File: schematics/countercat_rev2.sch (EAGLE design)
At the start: 67 parts, among them IC1 74LS595N, Q1 IRF520, Q2 2N3904, Q3 IRF520, Q4 IRF520, Q5 IRF520, U4 ATMEGA328P_PDIP, U6 RELAYPTH3, Y1 16MHz

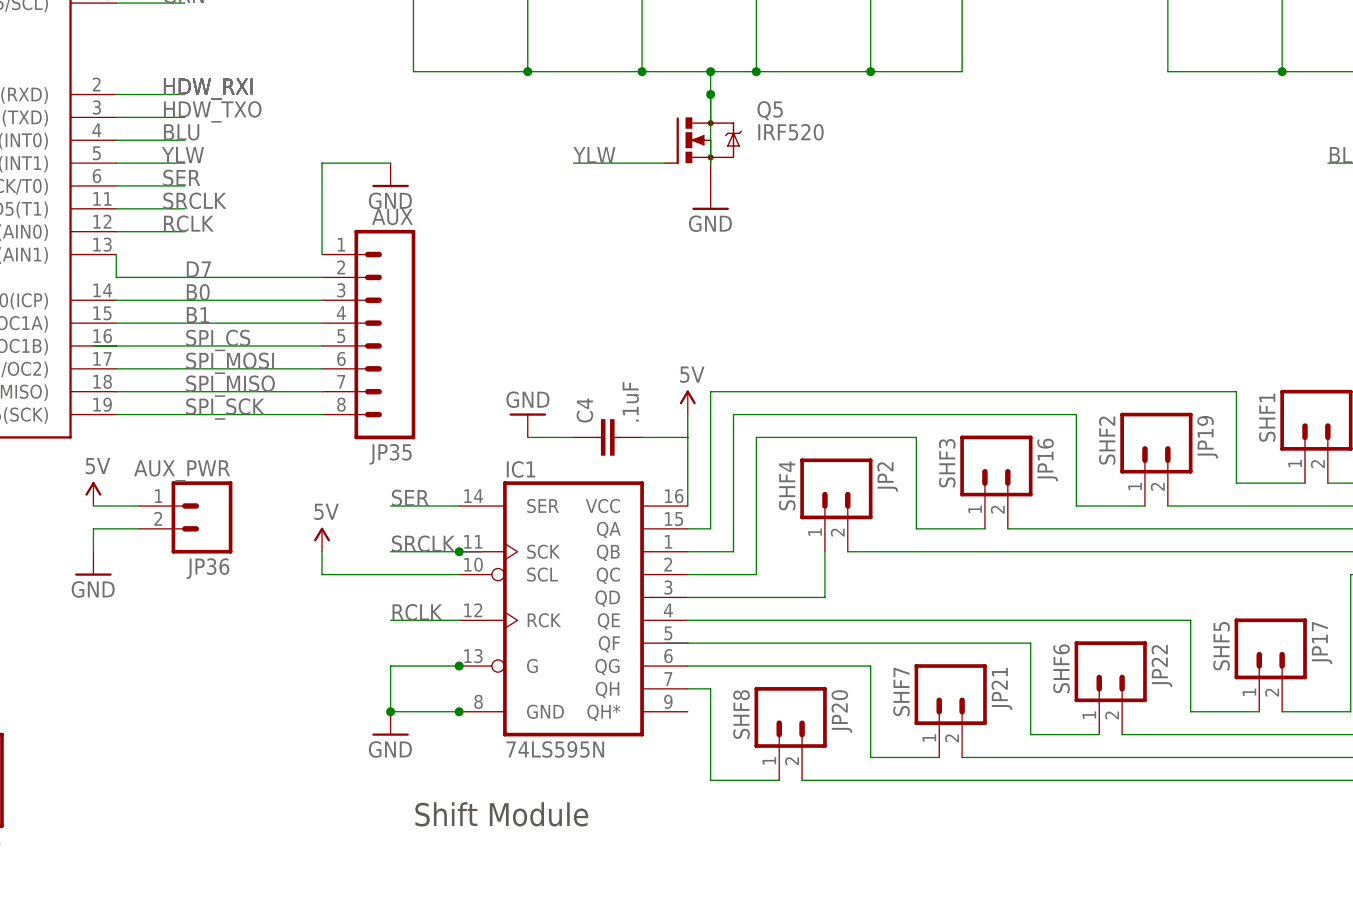
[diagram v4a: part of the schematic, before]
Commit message: Autorouted and DRC'd
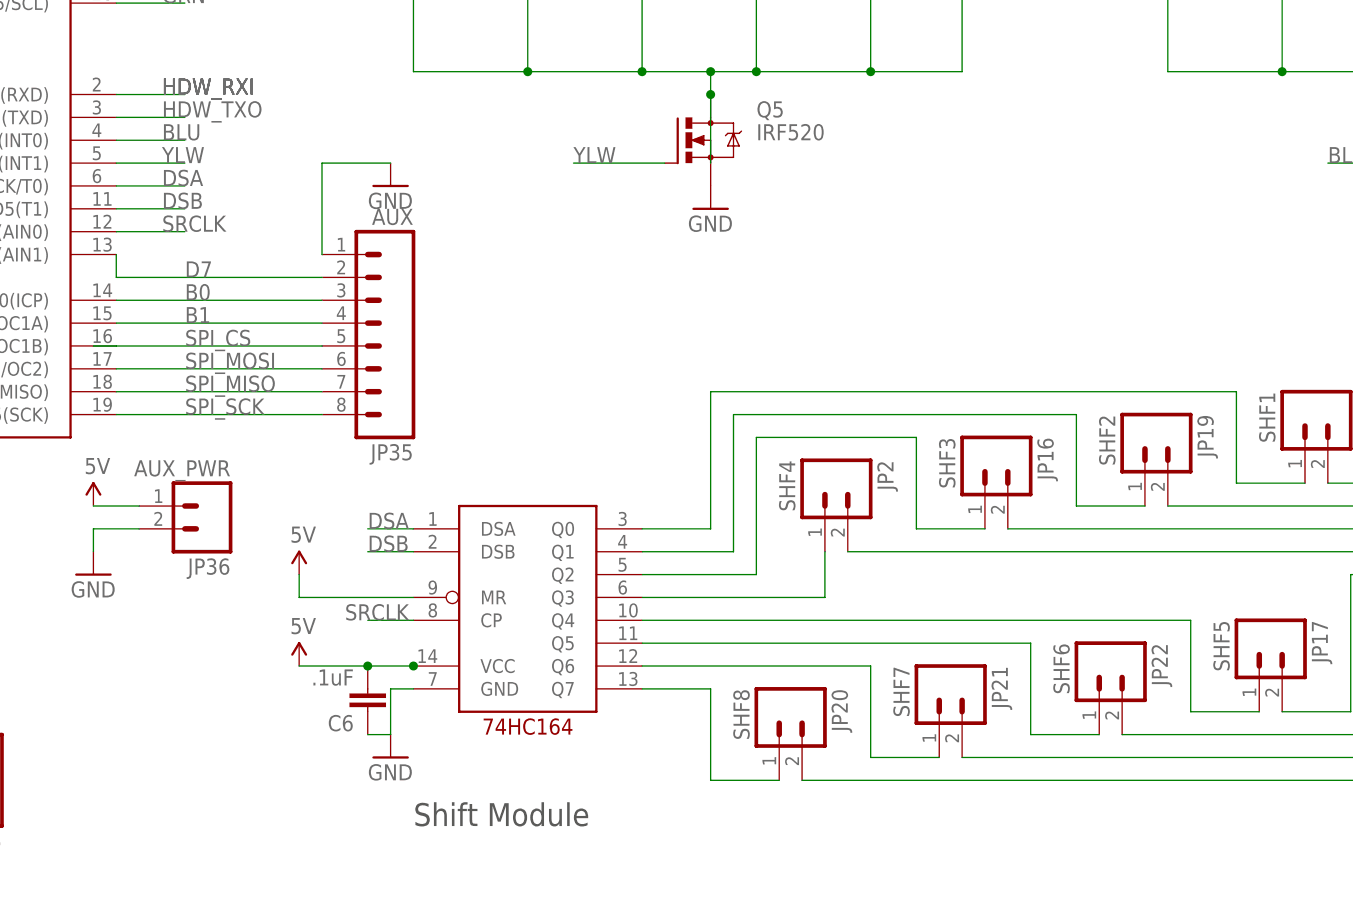
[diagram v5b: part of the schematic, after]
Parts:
- removed C4: .1uF, SparkFun-Capacitors:CAPPTH2
- removed IC1: 74LS595N, SparkFun-DigitalIC:74LS595N
- added C6: .1uF, SparkFun-Capacitors:CAPPTH2
- added U$15: 74XX164, andrews_eagle_lib:74XX164
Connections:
- removed net RCLK: IC1.RCK, U4.PD6(AIN0)
- removed net SER: IC1.SER, U4.PD4(XCK/T0)
- new net DSA: U$15.DSA, U4.PD4(XCK/T0)
- new net DSB: U$15.DSB, U4.PD5(T1)
- net 5V: now also C6.2, U$15.MR, U$15.VCC; no longer C4.2, IC1.SCL, IC1.VCC
- net GND: now also C6.1, U$15.GND; no longer C4.1, IC1.G, IC1.GND
- net N$1: now also U$15.Q4; no longer IC1.QE
- net N$26: now also U$15.Q0; no longer IC1.QA
- net N$27: now also U$15.Q1; no longer IC1.QB
- net N$28: now also U$15.Q2; no longer IC1.QC
- net N$29: now also U$15.Q3; no longer IC1.QD
- net N$30: now also U$15.Q6; no longer IC1.QG
- net N$31: now also U$15.Q5; no longer IC1.QF
- net N$32: now also U$15.Q7; no longer IC1.QH
- net SRCLK: now also U$15.CP, U4.PD6(AIN0); no longer IC1.SCK, U4.PD5(T1)

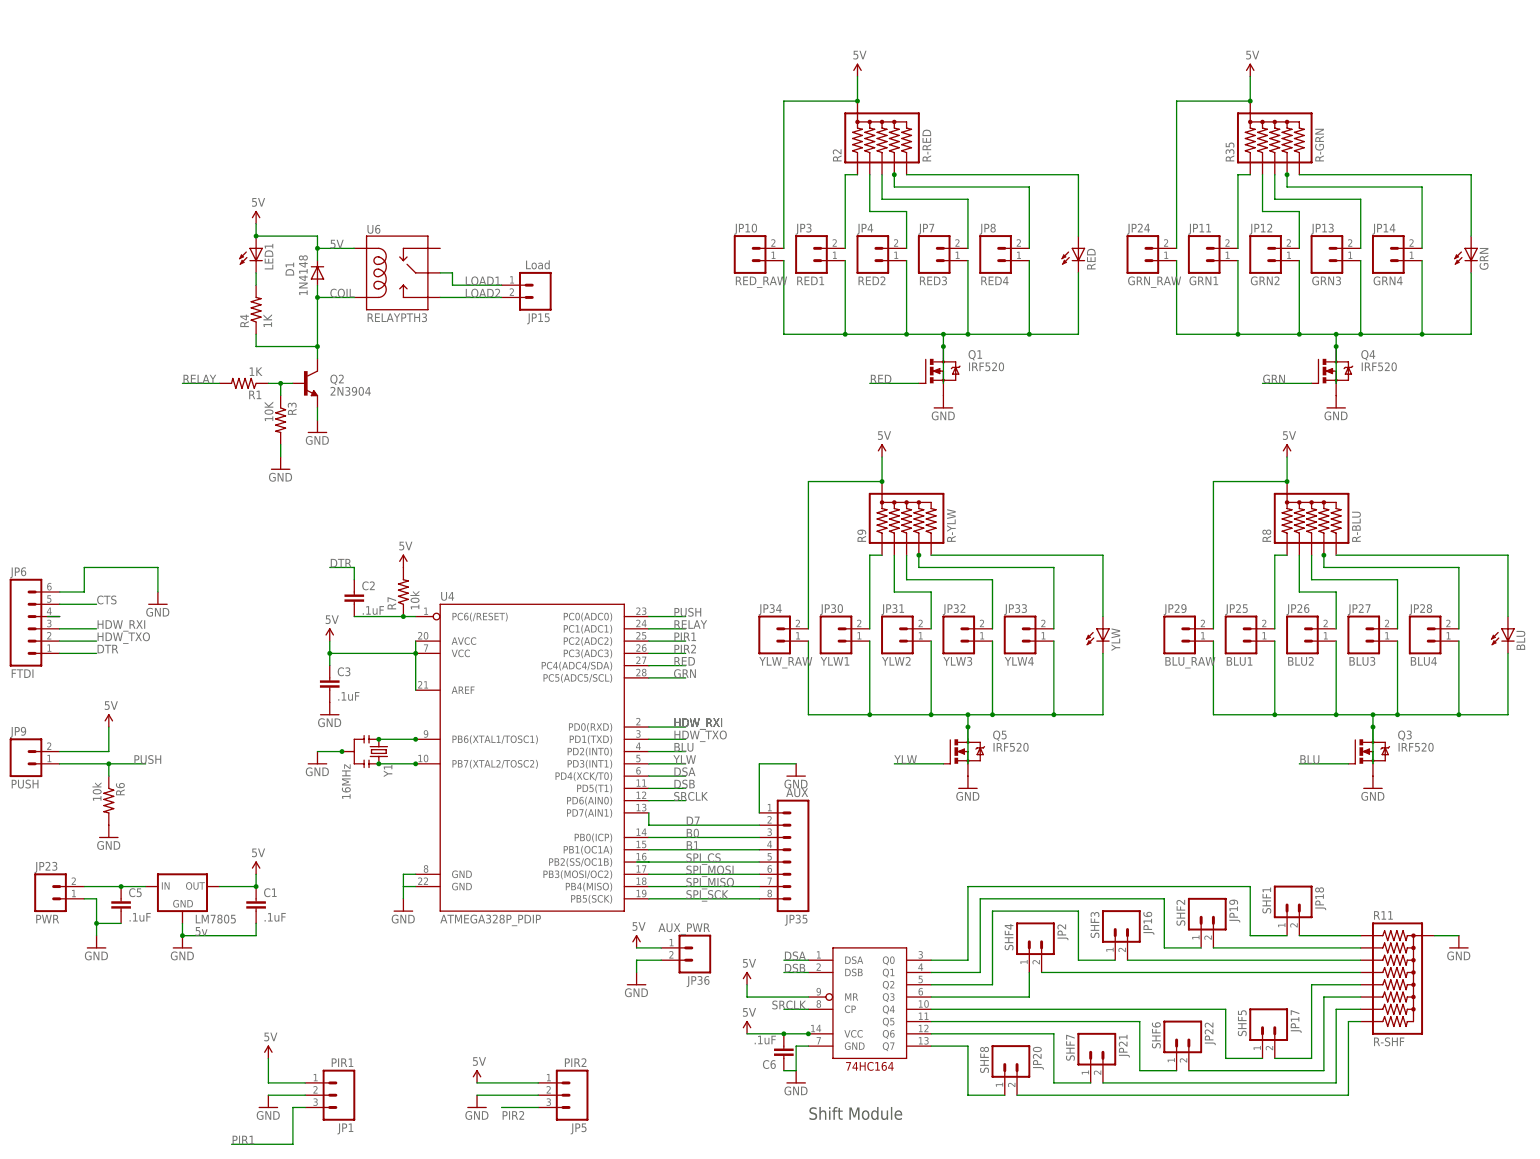
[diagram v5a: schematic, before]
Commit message: Got rid of relay on board. Made smaller, swapepd out shift reg. for decoder
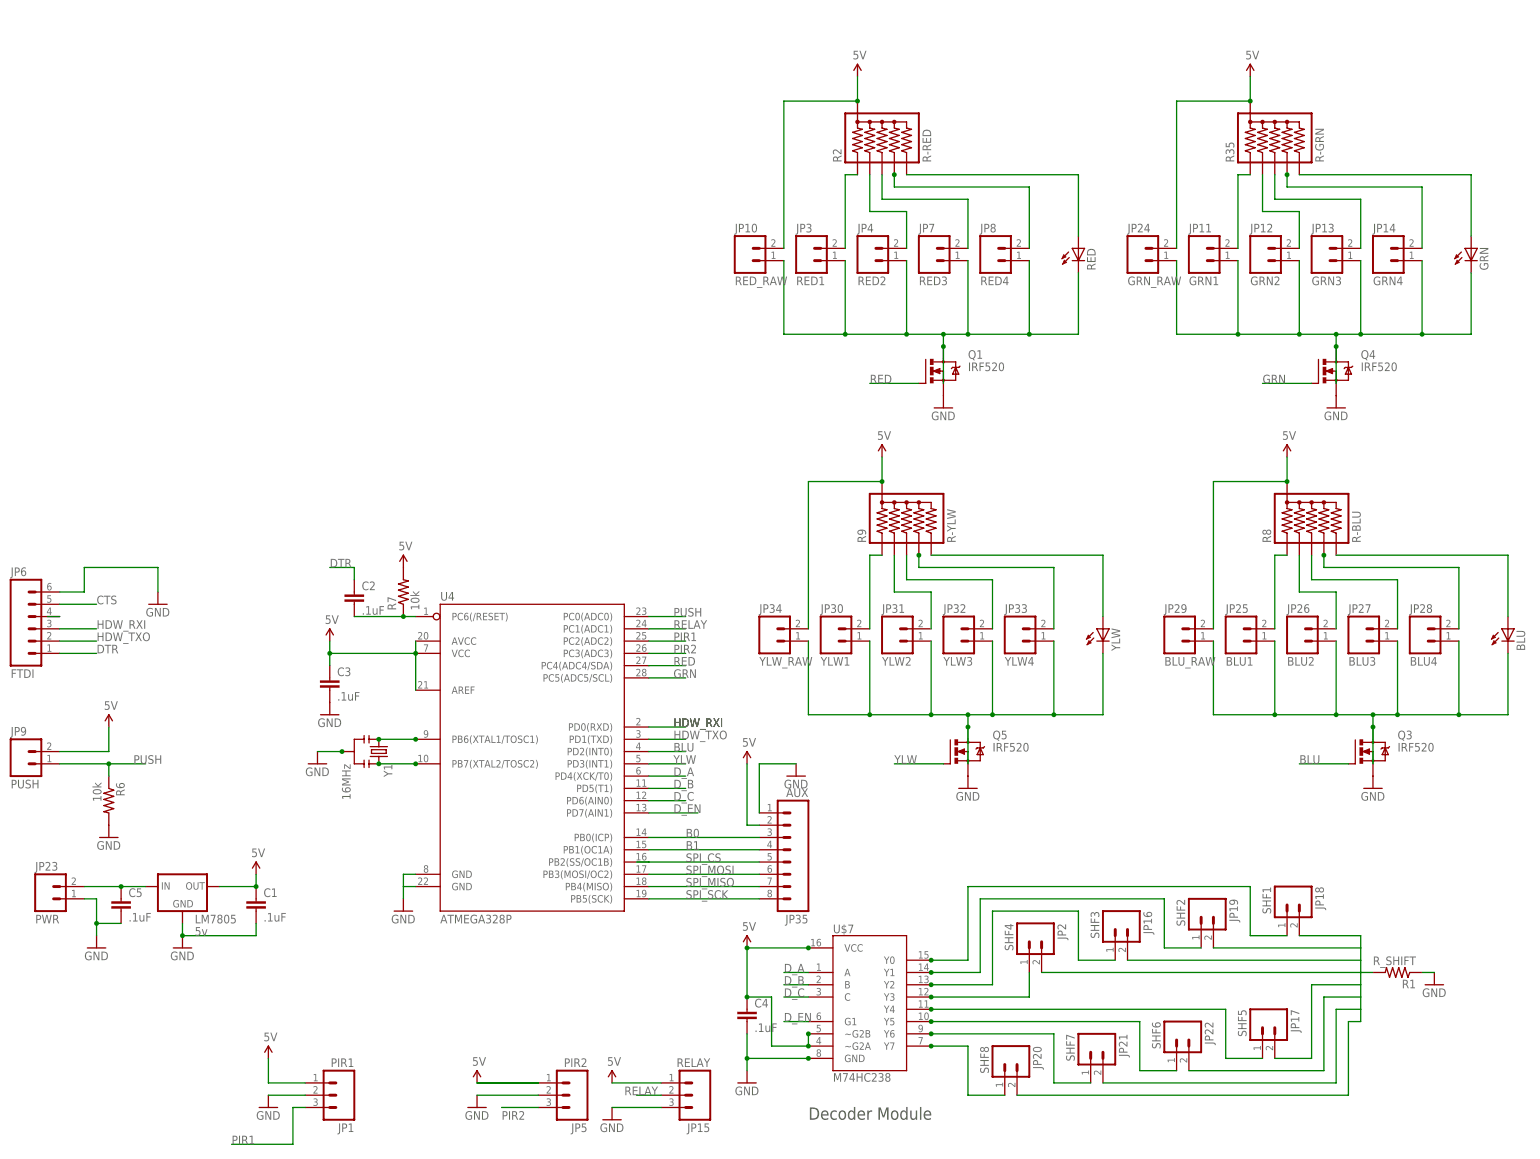
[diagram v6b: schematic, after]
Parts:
- removed C6: .1uF, SparkFun-Capacitors:CAPPTH2
- removed D1: 1N4148, SparkFun:DIODE1N4148
- removed JP36: AUX_PWR, SparkFun:M02POLAR
- removed LED1: (no value), SparkFun:LED5MM
- removed Q2: 2N3904, SparkFun:TRANSISTOR_NPNTO92
- removed R11: R-SHF, SparkFun-Resistors:RPACK-BUSSED-8-SIP-PTH-8
- removed R3: 10K, SparkFun-Resistors:RESISTORPTH-1/4W
- removed R4: 1K, SparkFun-Resistors:RESISTORPTH-1/4W
- removed U$15: 74XX164, andrews_eagle_lib:74XX164
- removed U6: RELAYPTH3, SparkFun:RELAYPTH3
- added C4: .1uF, SparkFun-Capacitors:CAPPTH2
- added U$7: M74HC238, SparkFun-DigitalIC:M74HC238
- JP15: value Load -> RELAY; device SparkFun:M025MM -> SparkFun:M03POLAR
- R1: value 1K -> R_SHIFT
- U4: value ATMEGA328P_PDIP -> ATMEGA328P
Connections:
- removed net COIL: D1.A, Q2.C, R4.1, U6.COIL2
- removed net D7: JP35.2, U4.PD7(AIN1)
- removed net DSA: U$15.DSA, U4.PD4(XCK/T0)
- removed net DSB: U$15.DSB, U4.PD5(T1)
- removed net LOAD1: JP15.1, U6.MAIN
- removed net LOAD2: JP15.2, U6.NO
- removed net N$10: JP18.2, R11.2
- removed net N$11: JP19.2, R11.3
- removed net N$14: JP16.2, R11.4
- removed net N$17: JP2.2, R11.5
- removed net N$20: JP17.2, R11.6
- removed net N$23: JP22.2, R11.7
- removed net N$24: JP21.2, R11.8
- removed net N$6: Q2.B, R1.1, R3.1
- removed net N$9: LED1.C, R4.2
- removed net SRCLK: U$15.CP, U4.PD6(AIN0)
- new net D_A: U$7.A, U4.PD4(XCK/T0)
- new net D_B: U$7.B, U4.PD5(T1)
- new net D_C: U$7.C, U4.PD6(AIN0)
- new net D_EN: U$7.G1, U4.PD7(AIN1)
- net 5V: now also C4.1, JP15.1, JP35.2, U$7.VCC, U$7.~G2A, U$7.~G2B; no longer C6.2, D1.C, JP36.1, LED1.A, U$15.MR, U$15.VCC, U6.COIL1
- net GND: now also C4.2, JP15.3, R1.1, U$7.GND; no longer C6.1, JP36.2, Q2.E, R11.1, R3.2, U$15.GND
- net N$1: now also U$7.Y4; no longer U$15.Q4
- net N$25: now also JP16.2, JP17.2, JP18.2, JP19.2, JP2.2, JP21.2, JP22.2, R1.2; no longer R11.9
- net N$26: now also U$7.Y0; no longer U$15.Q0
- net N$27: now also U$7.Y1; no longer U$15.Q1
- net N$28: now also U$7.Y2; no longer U$15.Q2
- net N$29: now also U$7.Y3; no longer U$15.Q3
- net N$30: now also U$7.Y6; no longer U$15.Q6
- net N$31: now also U$7.Y5; no longer U$15.Q5
- net N$32: now also U$7.Y7; no longer U$15.Q7
- net RELAY: now also JP15.2; no longer R1.2
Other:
- note added: "Decoder Module"
- note removed: "Shift Module"
- moved on the sheet: R1
